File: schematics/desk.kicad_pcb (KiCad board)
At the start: 2 copper layers, 194 x 150 mm, 34 parts, among them K1 energized = UP (raises desk), K2 energized = DOWN (lowers desk), Q1 IRLZ44N, Q2 2N7000, Q3 2N7000, Q4 BC337, Q5 BC327, U1 LM2596HV 29V-5V, U2 PinSocket_1x22_P2.54mm_Vertic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, U3 74HC123 250ms, U5 ACS724xLCTR-05AB, U6 74HC08

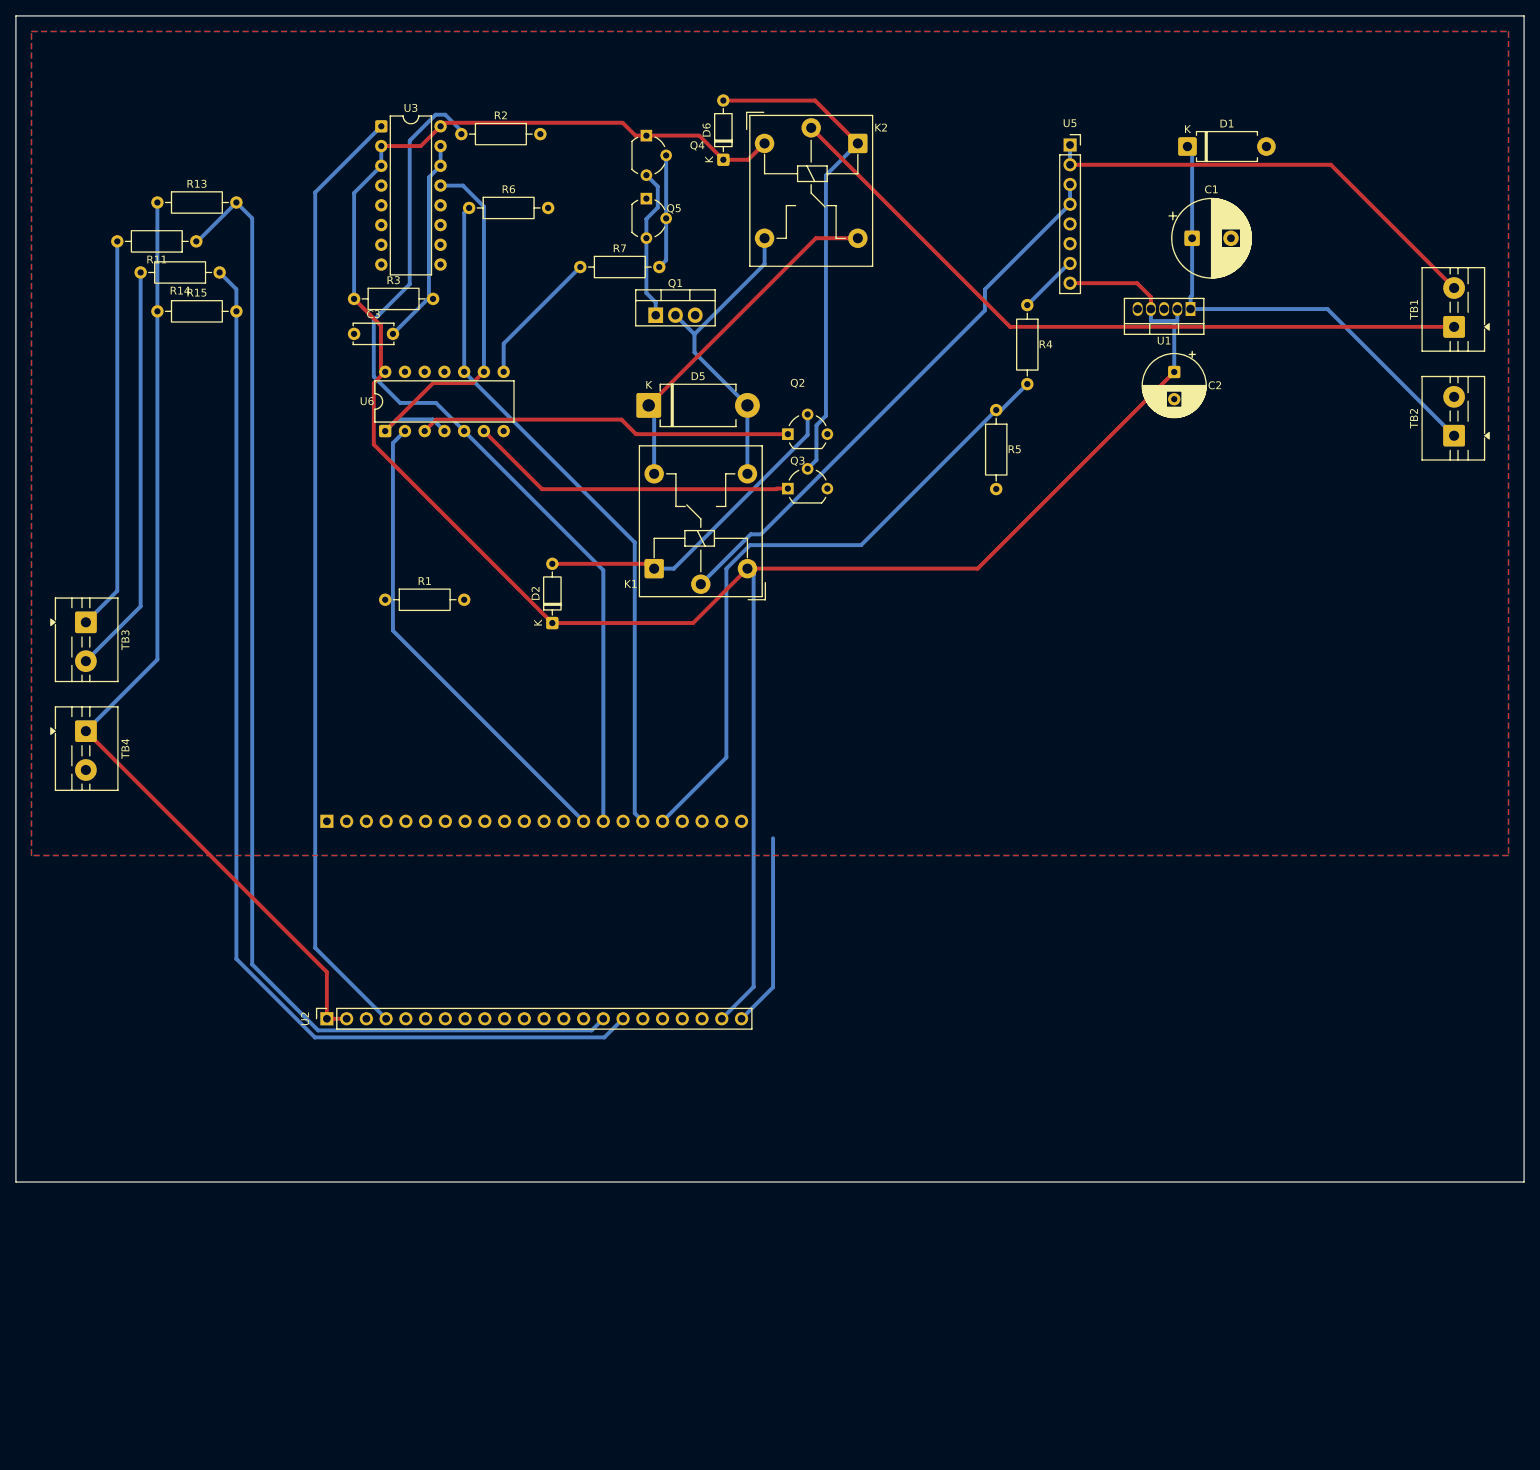
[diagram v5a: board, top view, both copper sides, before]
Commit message: Repack layout to fit a standard 10x15cm PCB blank
Previous layout was 194x150mm with a large empty region below the
main component cluster (also the cause of the incomplete-ground-fill
bug: the GND zone boundary was drawn to match the old, smaller board
and never widened when U2 was brought on-board, so it never covered
that area at all - see the intent behind the last commit's zone add,
which cloned that already-undersized boundary).

Rather than patch the boundary in place, redid placement from scratch:
grouped parts into functional clusters (power-in, U2 + gate/watchdog
logic, small pulldowns, FET drive, relays + current sense, motor-out
terminal) and packed them shelf-by-shelf into a 100x150mm outline,
rotating U3 and U5 90 degrees to cut their height contribution. Result
packs into 139x95mm of actual component area, comfortably inside the
100x150mm target with routing margin to spare.

Re-routed from scratch with Freerouting (2-layer, real netclass rules
patched into the DSN export) and refilled both ground pours sized to
the new, correct board outline.

12 vias (up from 0 on the oversized board - expected, there's a lot
less slack on a board less than 1/3 the area). 0 DRC violations, 0
unconnected - actually cleaner than the previous layout, which still
had 3 silkscreen overlaps and 4 thermal-relief warnings.

Single-sided component placement throughout; double-siding wasn't
needed once the real packing math was worked out (component bounding
boxes sum to ~7425mm2 against 15000mm2 available).
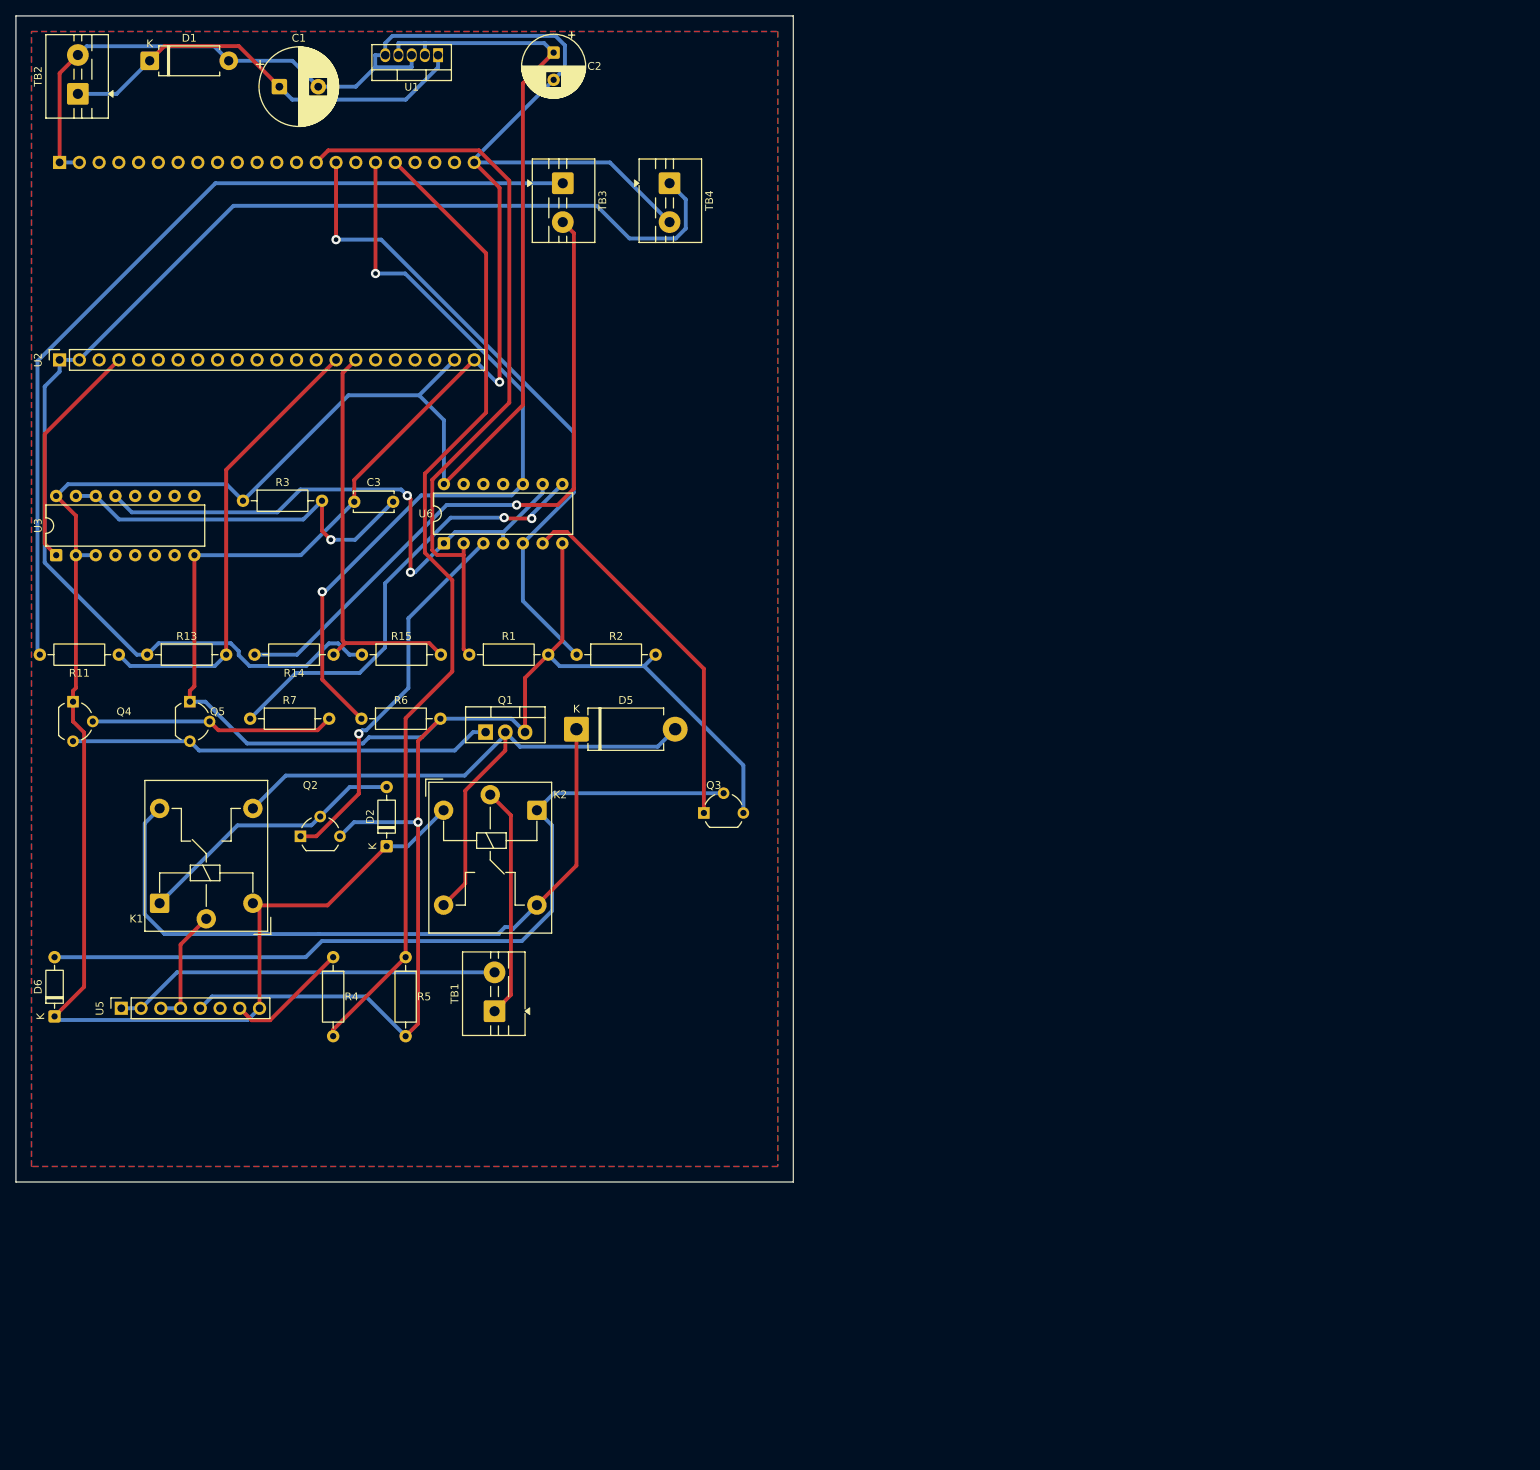
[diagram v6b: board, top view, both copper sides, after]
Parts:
- moved TB2 182.4 mm to (7.97, 10.0)
- moved U5 165.0 mm to (13.6, 127.7), turned to 90 degrees
- moved TB1 151.6 mm to (61.6, 128.0)
- moved D6 139.8 mm to (4.97, 128.7)
- moved D1 133.9 mm to (17.2, 5.77)
- moved R4 122.5 mm to (40.8, 121.1)
- moved C1 119.0 mm to (33.9, 9.10)
- moved Q4 103.6 mm to (7.34, 88.2)
- moved R5 103.6 mm to (50.1, 121.1)
- moved TB4 103.0 mm to (84.1, 21.5)
- moved U1 102.2 mm to (54.3, 5.05)
- moved K2 95.2 mm to (67.0, 102.2)
- moved U2 91.5 mm to (5.62, 44.2)
- moved C2 89.8 mm to (69.2, 4.72)
- moved Q5 87.4 mm to (22.4, 88.2)
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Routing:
- net GND: track 24.9 -> 438.8 mm, vias 0 -> 2
- net SW_UP: track 155.4 -> 58.8 mm
- net KICK: track 122.1 -> 29.7 mm
- net SW_DN: track 144.1 -> 52.3 mm
- net Net-(TB3-Pin_1): track 50.7 -> 114.9 mm
- net Net-(TB1-Pin_1): track 93.3 -> 29.8 mm
- net /DRV_UP: track 71.9 -> 15.4 mm
- net +3V3: track 124.2 -> 174.2 mm
- net VSW: track 44.9 -> 92.5 mm
- net /MRET: track 40.3 -> 85.7 mm
- net ISENSE: track 84.4 -> 128.3 mm
- net Net-(D6-A): track 64.1 -> 105.1 mm
- net Net-(R7-Pad1): track 17.6 -> 57.9 mm, vias 0 -> 2
- net DIR_A: track 62.0 -> 97.6 mm
- net Net-(Q1-G): track 19.7 -> 54.5 mm
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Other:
- board size 194 x 150 mm -> 100 x 150 mm

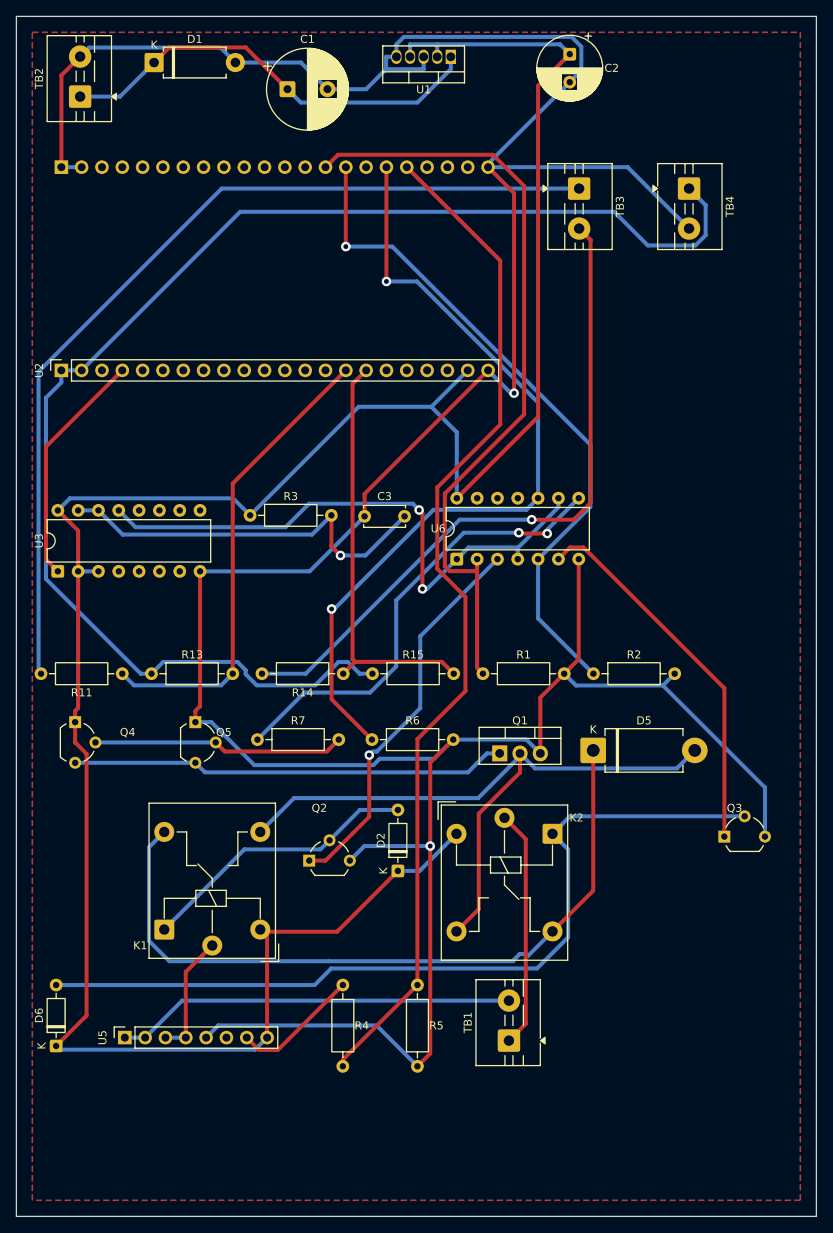
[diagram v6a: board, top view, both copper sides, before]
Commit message: Compact layout further: 100x150mm -> 88x123mm
Three specific issues from eyeballing the previous layout, all fixed:

1. U2's Value text field still read "PinSocket_1x22_P2.54mm_Vertical" -
   a leftover from the base footprint it was cloned from - rotated
   90 degrees and long enough to stretch U2's bounding box 11mm past
   its real physical extent (39.4mm tall vs the actual ~28mm). Every
   placement decision involving U2, including the whole previous
   packing pass, was working off that inflated size. Renamed to
   "ESP32_DevKitC" and put it back inside the footprint's real bounds.
   This alone explains why the U2-to-U3/U6 gap looked bigger than the
   configured 1.8mm shelf spacing.

2. Q3 was the single rightmost feature on the old board (sitting to
   the right of K2), while the shelf below it (D6/U5/R4/R5/TB1) had
   30mm of unused width. Moved Q3 onto that shelf instead - it's a
   small 2N7000, doesn't affect that shelf's height - which let the
   board width follow TB4 instead (was the actual bottleneck once Q3
   moved).

3. The last row of components ended 15mm above the old board's bottom
   edge - a leftover from originally sizing the outline to the target
   10x15cm blank rather than the real packed height. Outline now
   follows the actual packed extent (plus a small margin) instead of
   a fixed target size.

Also tightened inter-shelf gaps from 2.0mm to 1.2-1.5mm.

Re-routed from scratch with Freerouting and refilled both ground
pours to match the new outline. 6 vias (down from 12 - the tighter
placement gave the router shorter, more direct paths). 0 unconnected,
2 starved-thermal warnings (same cosmetic category as before, not a
connectivity issue).
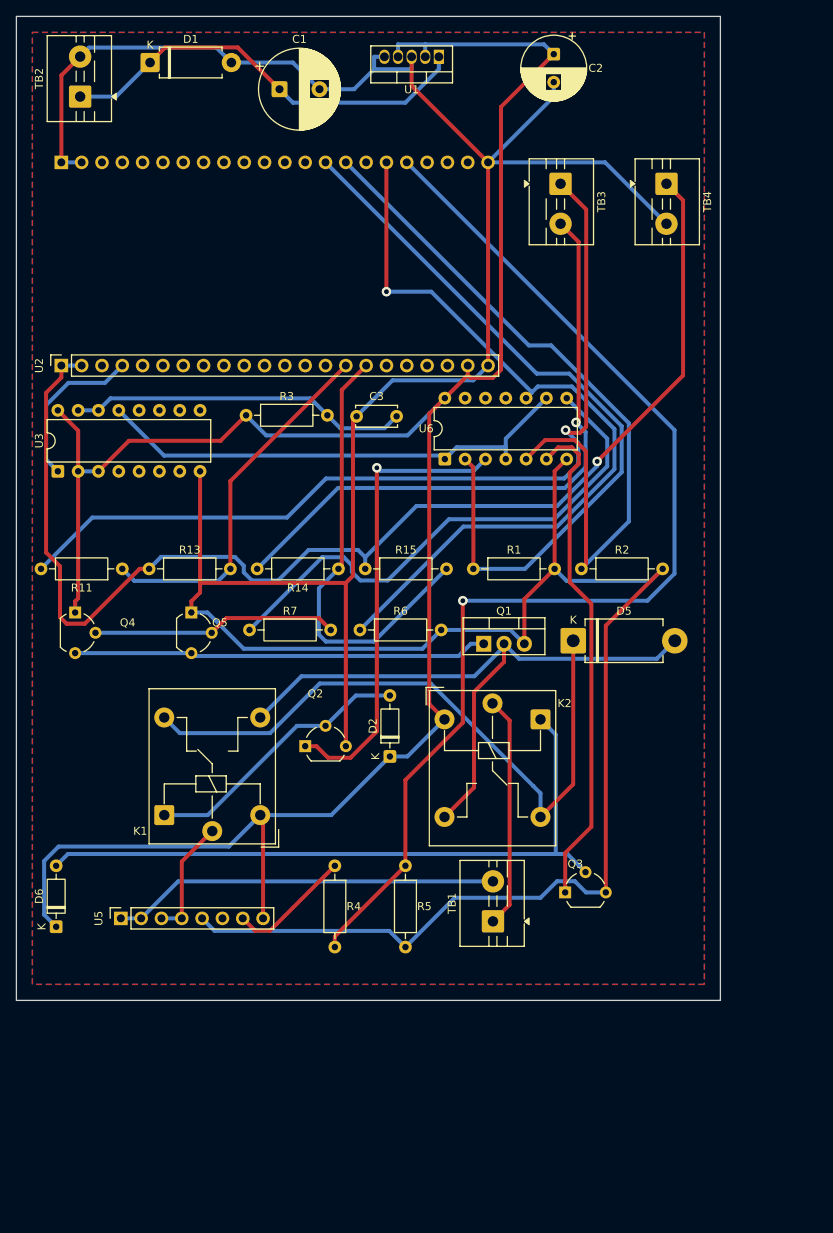
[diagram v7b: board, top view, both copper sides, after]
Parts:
- U2: value PinSocket_1x22_P2.54mm_Vertical -> ESP32_DevKitC
- moved Q3 21.1 mm to (68.6, 109.5)
- moved TB1 15.0 mm to (59.6, 113.1)
- moved R5 15.0 mm to (48.6, 106.2)
- moved R4 14.9 mm to (39.8, 106.2)
- moved U5 14.9 mm to (13.1, 112.7)
- moved D6 14.9 mm to (4.97, 113.8)
- moved K2 14.4 mm to (65.5, 87.9)
- moved D2 14.3 mm to (46.7, 92.5)
- moved Q2 14.3 mm to (36.1, 91.2)
- moved K1 14.3 mm to (18.5, 99.8)
- moved D5 13.9 mm to (69.6, 78.0)
- moved Q1 13.9 mm to (58.4, 78.4)
- moved R6 13.8 mm to (42.9, 76.7)
- moved R7 13.7 mm to (29.1, 76.7)
- moved Q5 13.7 mm to (21.9, 74.5)
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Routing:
- net +5V: track 300.9 -> 274.4 mm
- net Net-(D6-A): track 105.1 -> 85.3 mm
- net +3V3: track 174.2 -> 156.9 mm, vias 0 -> 1
- net Net-(Q3-G): track 47.2 -> 62.7 mm
- net ISENSE: track 128.3 -> 143.1 mm, vias 0 -> 1
- net SW_UP: track 58.8 -> 46.1 mm
- net /WDOG: track 73.8 -> 61.2 mm, vias 2 -> 0
- net VSW: track 92.5 -> 82.8 mm
- net GND: track 438.8 -> 429.4 mm, vias 2 -> 0
- net Net-(Q2-G): track 48.9 -> 58.2 mm
- net KICK: track 29.7 -> 20.4 mm
- net Net-(R7-Pad1): track 57.9 -> 66.7 mm, vias 2 -> 0
- net DIR_B: track 84.9 -> 93.5 mm, vias 1 -> 0
- net Net-(U3A-Cext): track 49.4 -> 42.6 mm, vias 1 -> 0
- net Net-(TB3-Pin_2): track 84.8 -> 78.3 mm
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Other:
- board size 100 x 150 mm -> 88 x 123 mm
